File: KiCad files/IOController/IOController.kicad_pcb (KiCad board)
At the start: 2 copper layers, 85.5 x 30 mm, 46 parts, among them IC1 TPS923654DMTR, J1 AVR-ISP-6, J101 Conn_01x04, J2 XT60 Horizontal Socket, J3 Conn_01x04, SW1 EC12, SW101 B3U, SW102 B3U, SW103 B3U, SW104 B3U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

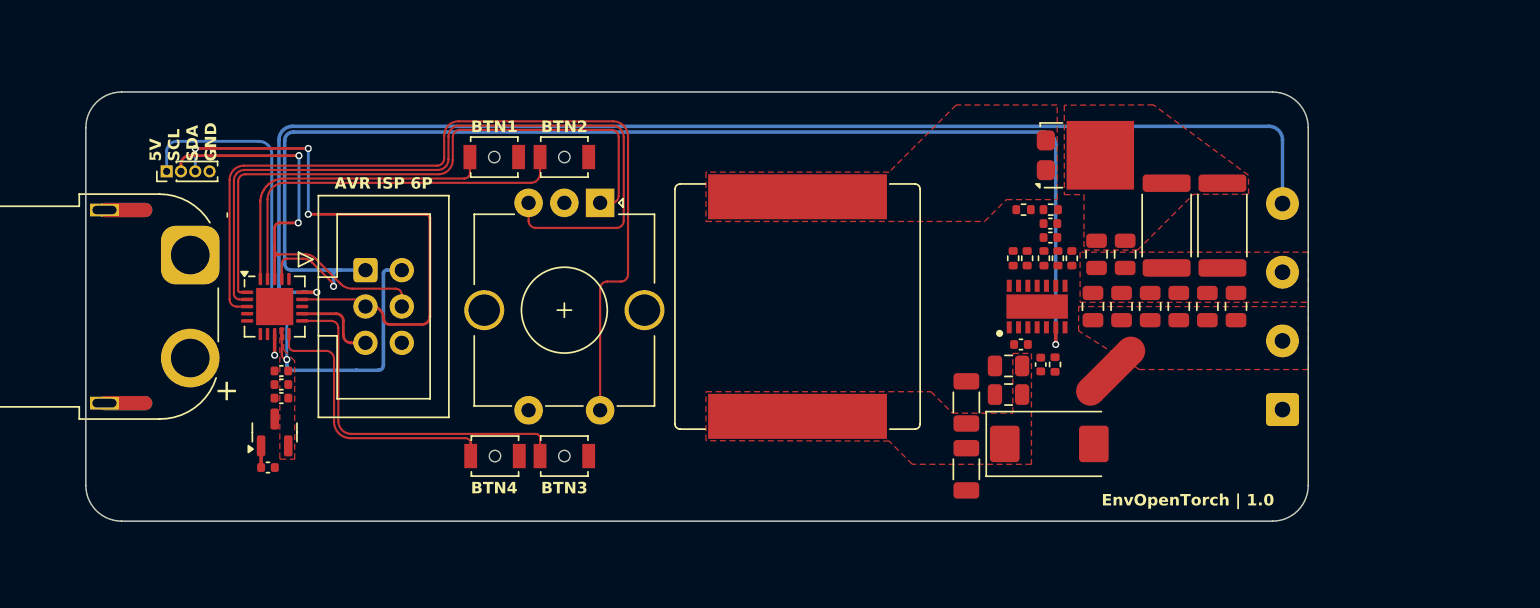
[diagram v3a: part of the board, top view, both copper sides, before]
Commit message: modified design to be closer to reference version.
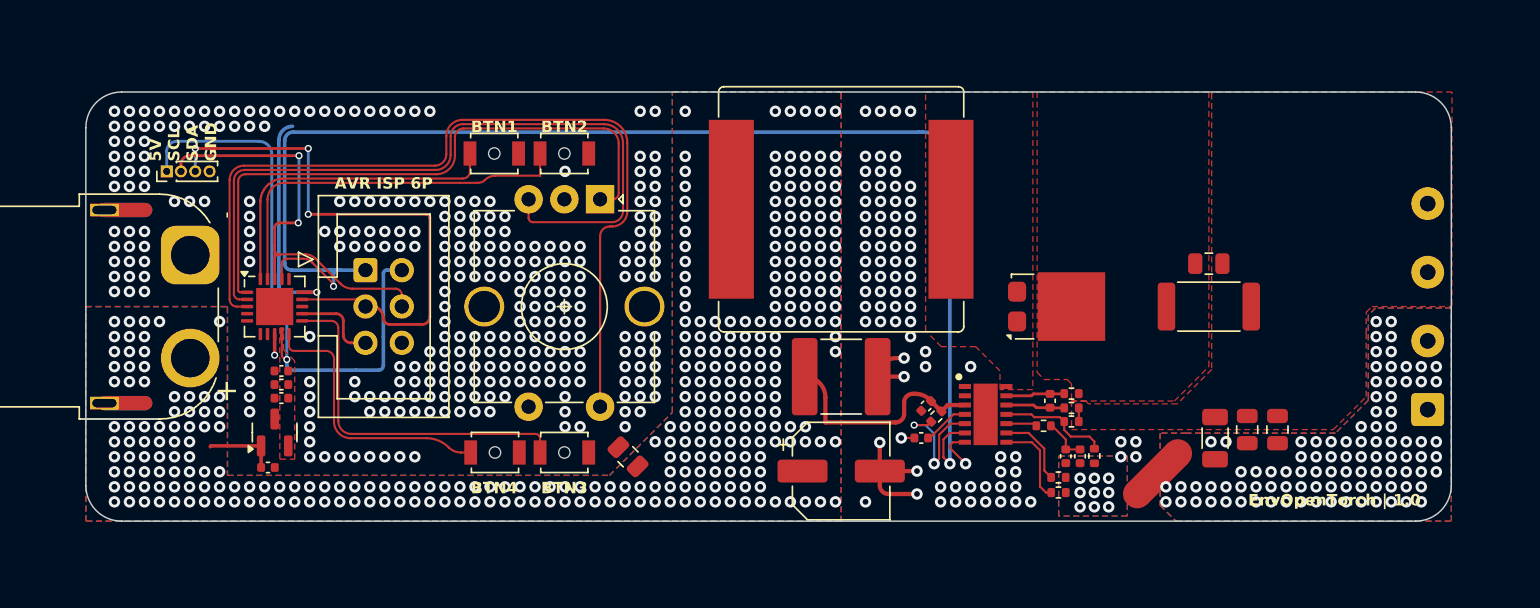
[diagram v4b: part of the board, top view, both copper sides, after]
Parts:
- removed C10, C11, C22, C23: 50V 100nF 0805, Capacitor_SMD:C_0805_2012Metric
- removed C21: 50V 1uF 0805, Capacitor_SMD:C_0805_2012Metric
- removed C9: 35V 22uF 1206, Capacitor_SMD:C_1206_3216Metric
- removed R14: 2512 120mR, Resistor_SMD:R_2512_6332Metric
- added C5: 50V 0.1uF 0805, Capacitor_SMD:C_0805_2012Metric, F.Cu at (77.9, 42.0)
- C14: value 50V 0.1uF 0805 -> 16V 0.1uF 0402; footprint Capacitor_SMD:C_0805_2012Metric -> Capacitor_SMD:C_0402_1005Metric
- C18: value 50V 2.2uF 0805 -> 100V 0.1uF 0805
- C19: value 50V 2.2uF 0805 -> 100V 1uF 0805
- C20: value 50V 1uF 0805 -> 100V 2.2uF 1205; footprint Capacitor_SMD:C_0805_2012Metric -> Capacitor_SMD:C_1206_3216Metric
- C7: value 35V 68uF -> 50V 68uF; footprint Capacitor_Tantalum_SMD:CP_EIA-7343-43_Kemet-X -> Capacitor_SMD:CP_Elec_6.3x3
- C8: value 35V 22uF 1206 -> 50V 22uF 2220; footprint Capacitor_SMD:C_1206_3216Metric -> Capacitor_SMD:C_2220_5750Metric
- L1: value SRP1770TA-100M -> SRP1770TA-220M
- R10: value Rovp1 200K 0402 -> Rovp1 500K 0402
- R9: value 2512 120mR -> 2512 33mR
- moved R11 17.5 mm to (110.5, 41.9), turned to 90 degrees
- moved R7 16.4 mm to (108.0, 44.5), turned to 0 degrees
- moved C15 16.4 mm to (109.5, 42.0), turned to -90 degrees
- moved C18 15.5 mm to (123.3, 40.1)
- moved C16 15.3 mm to (108.5, 42.0), turned to -90 degrees
- moved R6 15.3 mm to (108.0, 43.4), turned to 0 degrees
- moved R10 15.2 mm to (108.9, 39.5), turned to 0 degrees
- moved C7 14.7 mm to (92.8, 43.0)
- moved R8 11.7 mm to (107.0, 39.8), turned to 0 degrees
- moved R13 10.9 mm to (108.9, 38.6), turned to 0 degrees
- moved D1 10.8 mm to (107.9, 31.5)
- moved C14 10.7 mm to (107.4, 38.1), turned to 90 degrees
- moved R12 10.3 mm to (108.9, 37.6), turned to 0 degrees
- moved J101 10.2 mm to (133.8, 38.7)
- moved C13 9.80 mm to (98.4, 40.7), turned to 0 degrees
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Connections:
- C14 pad 1: Net-(D1-K) -> /LED Driver/CSP
- C14 pad 2: LED V+ -> /LED Driver/CSN
- IC1 pad 12: Net-(IC1-CSP) -> /LED Driver/CSP
- IC1 pad 13: Net-(IC1-CSN) -> /LED Driver/CSN
- R12 pad 1: Net-(IC1-CSN) -> /LED Driver/CSN
- R13 pad 1: Net-(IC1-CSP) -> /LED Driver/CSP
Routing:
- net therm1_adc: track 89.7 -> 15.6 mm
- net VCC: track 1.51 -> 20.9 mm, vias 0 -> 310
- net GND: track 1.47 -> 18.2 mm, vias 1 -> 376
- net Net-(IC1-ADIM/HD): track 0.00 -> 9.33 mm, vias 0 -> 2
- net Net-(IC1-UVP): track 0.00 -> 7.78 mm
- net Net-(IC1-TEMP): track 0.00 -> 6.07 mm
- net Net-(IC1-FSET): track 0.00 -> 5.28 mm
- net /LED Driver/CSP: track 0.00 -> 4.12 mm
- net /LED Driver/CSN: track 0.00 -> 4.10 mm
- net Net-(IC1-VCC): track 0.00 -> 3.25 mm
- net Net-(C15-Pad1): track 0.00 -> 3.13 mm
- net LED_PWM_5V: track 92.0 -> 94.8 mm
- net Net-(IC1-COMP): track 0.00 -> 2.15 mm
- net LED V+: track 0.00 -> 0.95 mm
- net BTN5: track 61.8 -> 60.9 mm
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- added copper zone on B.Cu, net LED_V-
- added copper zone on B.Cu, net VCC
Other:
- board size 85.5 x 30 mm -> 95.4 x 30 mm

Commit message: made a few small fixes.
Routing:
- net VCC: vias 310 -> 173
- net LED_V-: vias 95 -> 49
- net LED V+: vias 0 -> 147
- net GND: vias 376 -> 43
- added copper zone on B.Cu, net LED V+

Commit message: corrected a few things to make life a bit easier.
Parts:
- IC1: footprint TPS922054DMTR:SON65P300X450X100-15N-D -> Package_SON:VSON-14-1EP_3x4.45mm_P0.65mm_EP1.6x4.2mm_ThermalVias
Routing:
- net VCC: vias 173 -> 0
- net LED_V-: vias 49 -> 0
- net LED V+: vias 147 -> 0
- net GND: vias 43 -> 131
- removed copper zone on B.Cu, net VCC
